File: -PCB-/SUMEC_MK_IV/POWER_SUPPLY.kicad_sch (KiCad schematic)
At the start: 28 parts, among them IC1 TPS565242DRLR, J1 XT30PW-M, Q1 PMOS, SW1 SW_DPDT_x2, U1 TPS62133, U2 LM1084-3.3

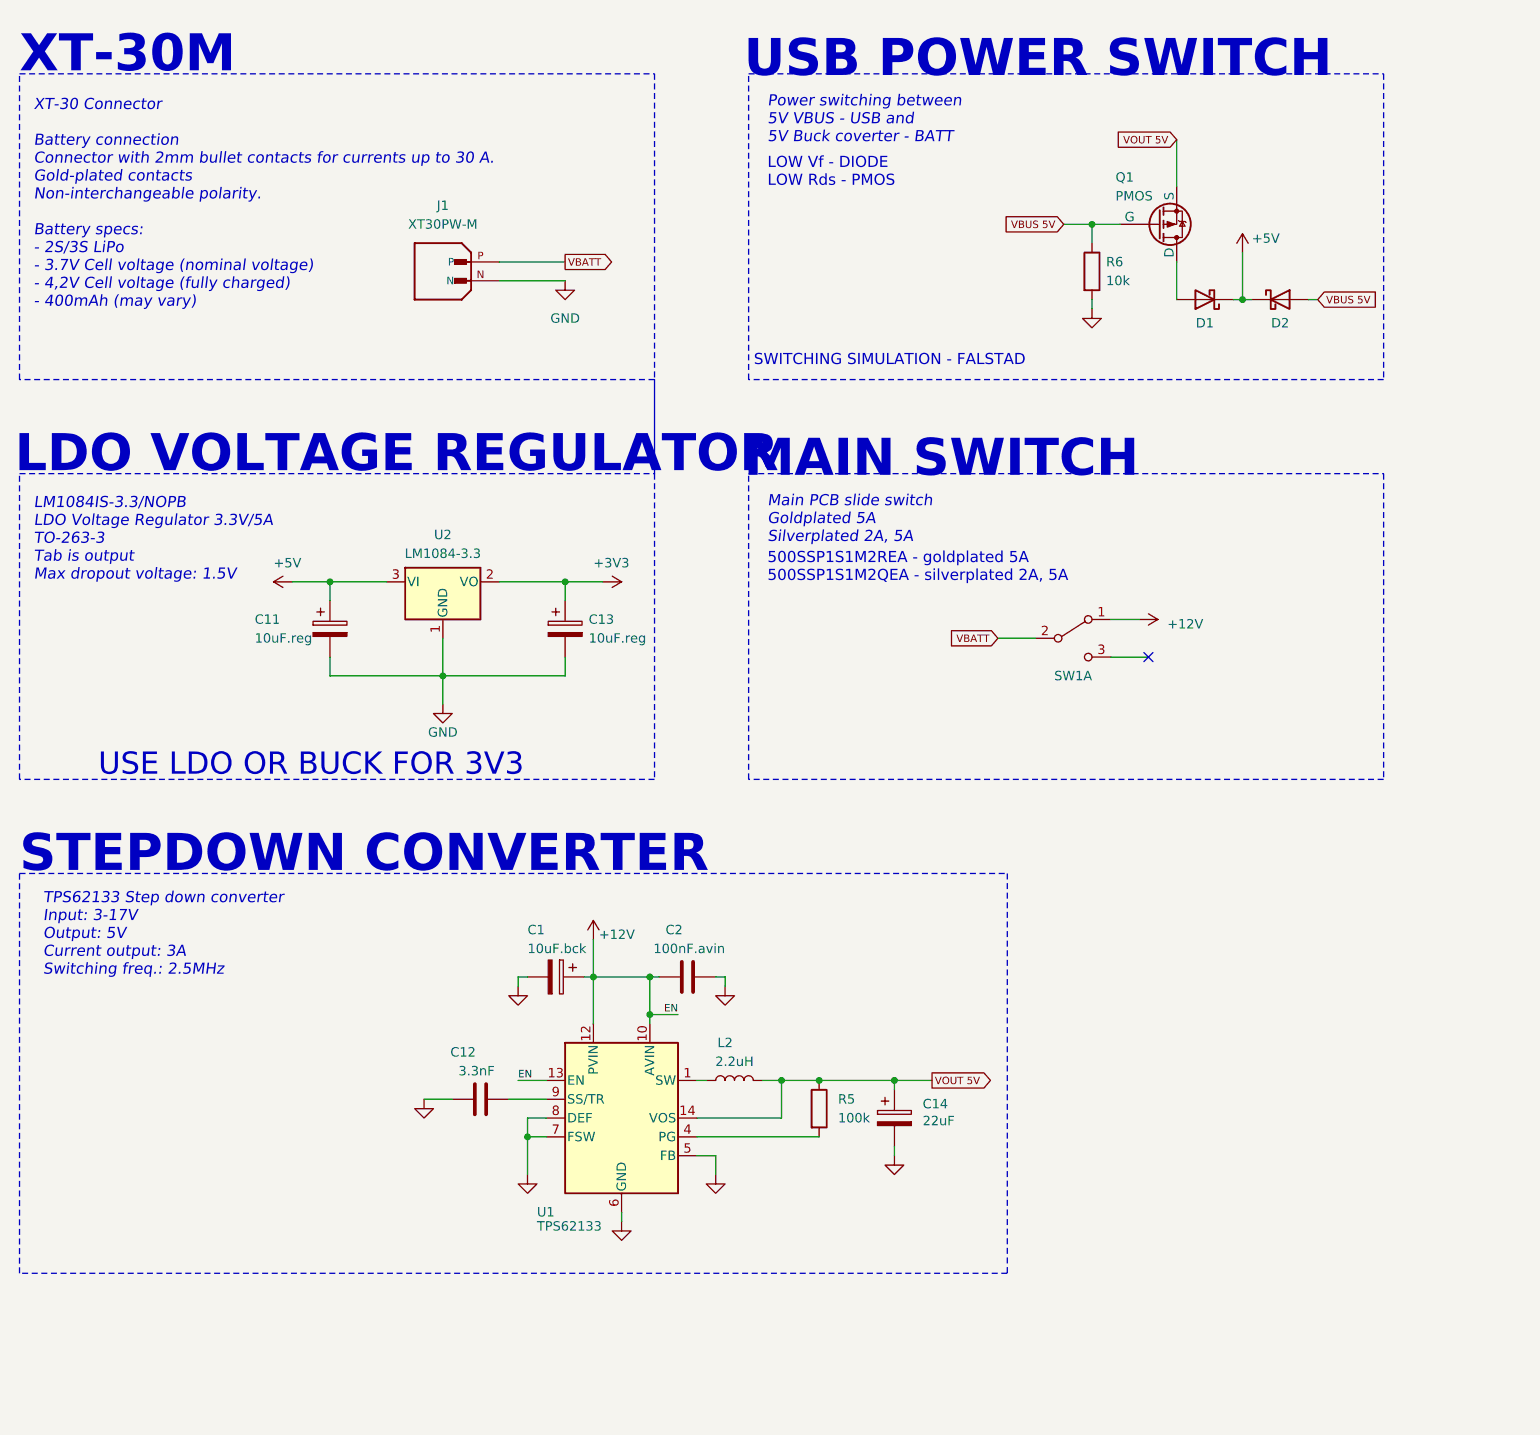
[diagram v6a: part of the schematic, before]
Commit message: MK4 schematic update
Almost done. Did some work on motor drivers, should be final now. Sensors sheet is almost done - object detecting missing. MCU sheet - missing. but yeah. almost done.
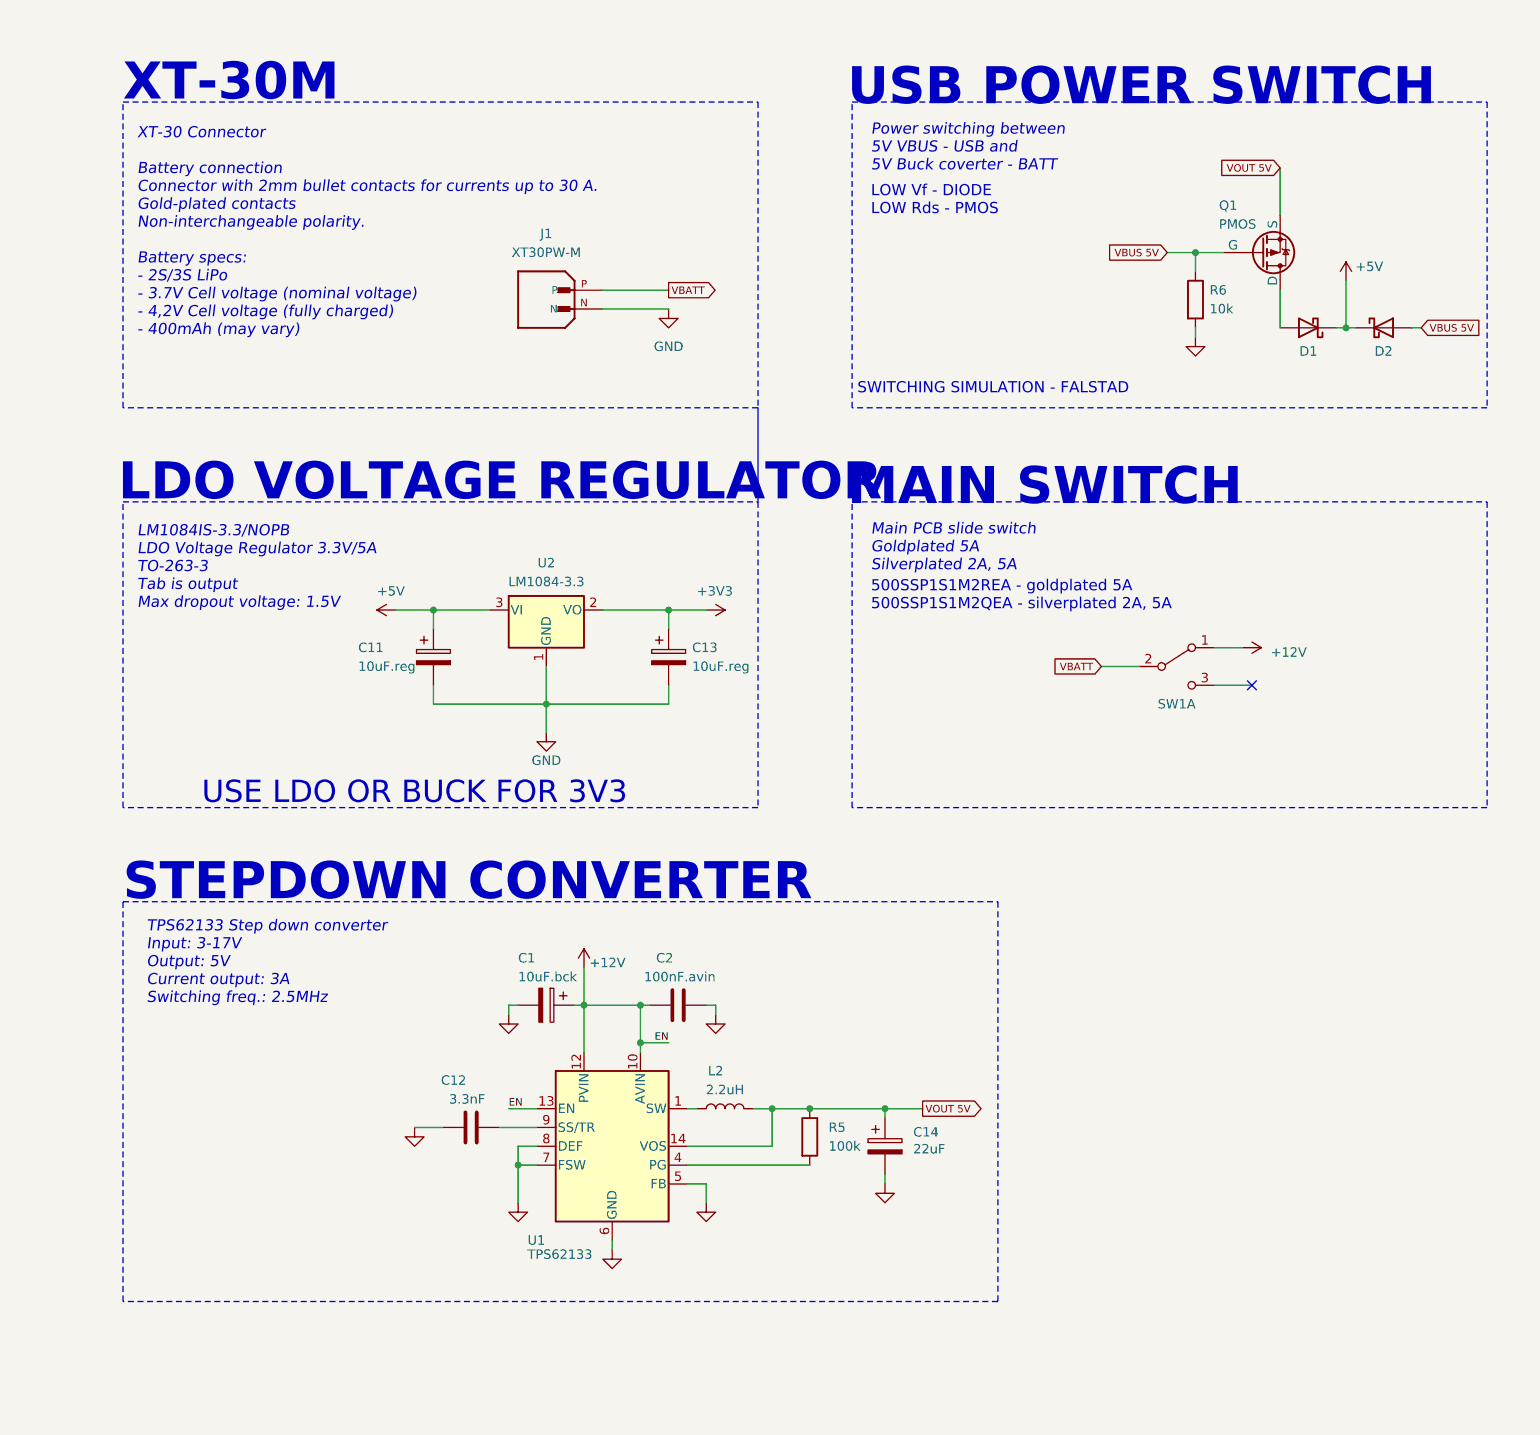
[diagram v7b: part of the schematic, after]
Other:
- moved on the sheet: C1, C11, C12, C13, C14, C2, D1, D2, J1, L2, Q1, R5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

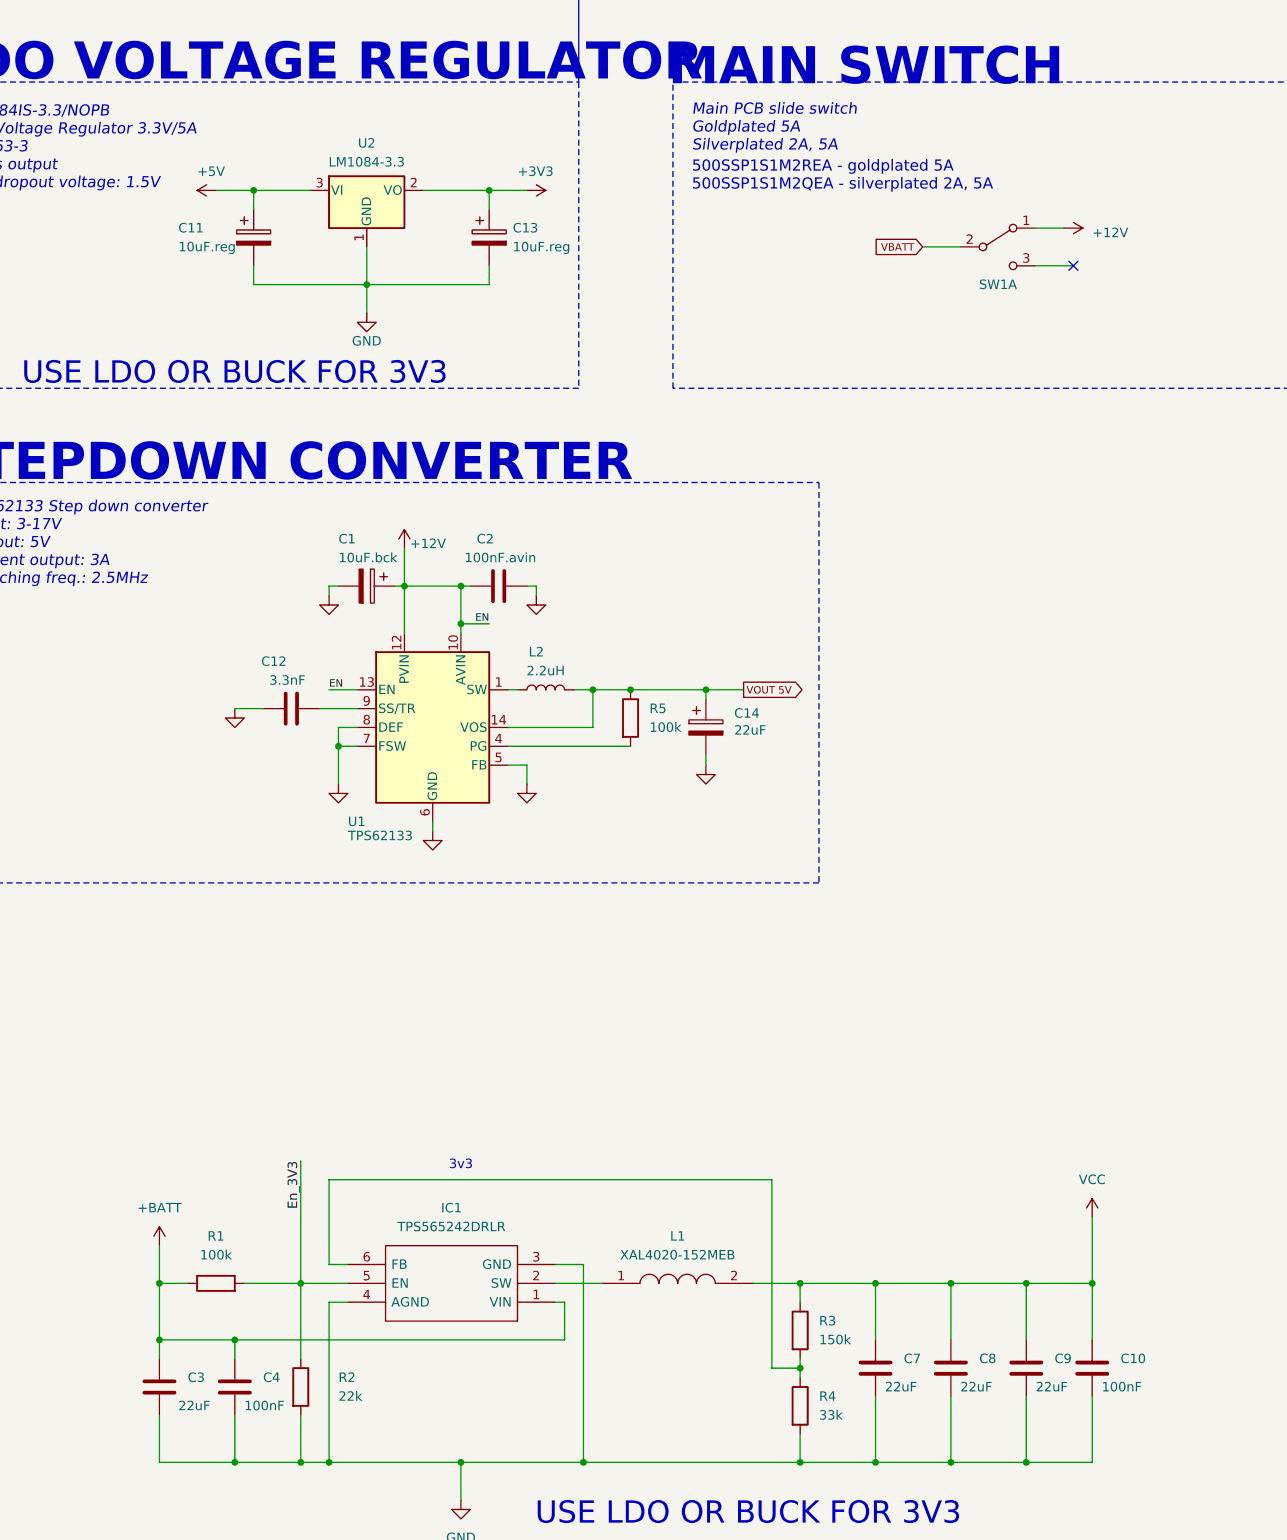
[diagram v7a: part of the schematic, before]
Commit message: MKIV major update
Updated everything, custom symbol for ESP32, MCU sheet done, new test points added, motor control revision.

all left is to clean it up a bit
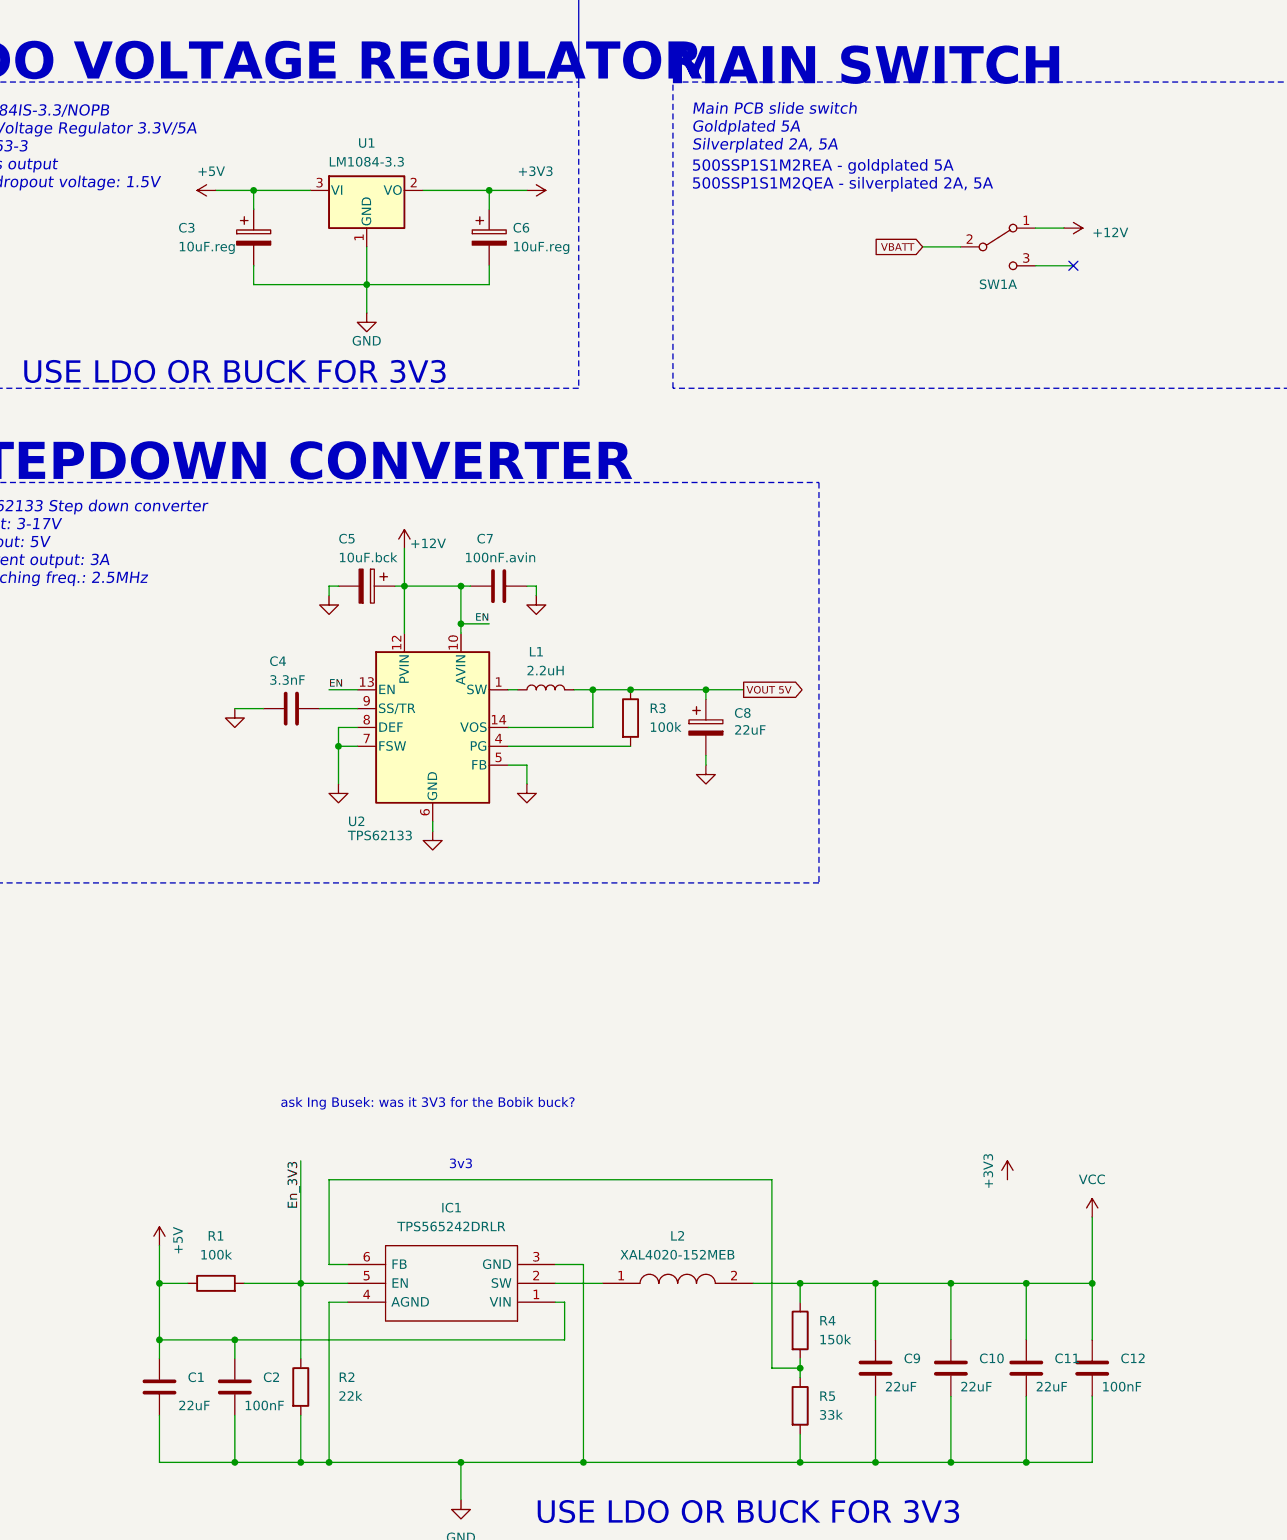
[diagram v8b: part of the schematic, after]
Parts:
- renumbered C3 to C1, C8 to C10, C9 to C11, C10 to C12, C4 to C2, C11 to C3, C12 to C4, C1 to C5, C13 to C6, C2 to C7, C14 to C8, C7 to C9, L2 to L1, L1 to L2, R5 to R3, R3 to R4, R4 to R5, U2 to U1, U1 to U2
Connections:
- net +BATT is gone; now on net +5V: C1.1, C2.1, IC1.1 (VIN), R1.1
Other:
- note added: "ask Ing Busek: was it 3V3 for the Bobik buck?"
